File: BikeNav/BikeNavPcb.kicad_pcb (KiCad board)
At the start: 2 copper layers, 12 parts, among them J9 1.8 TFT SPi 128x160 pins, SW1 SW_DPST_x2, U1 TP4056, U2 ESP32-C3_SUPERMINI_TH

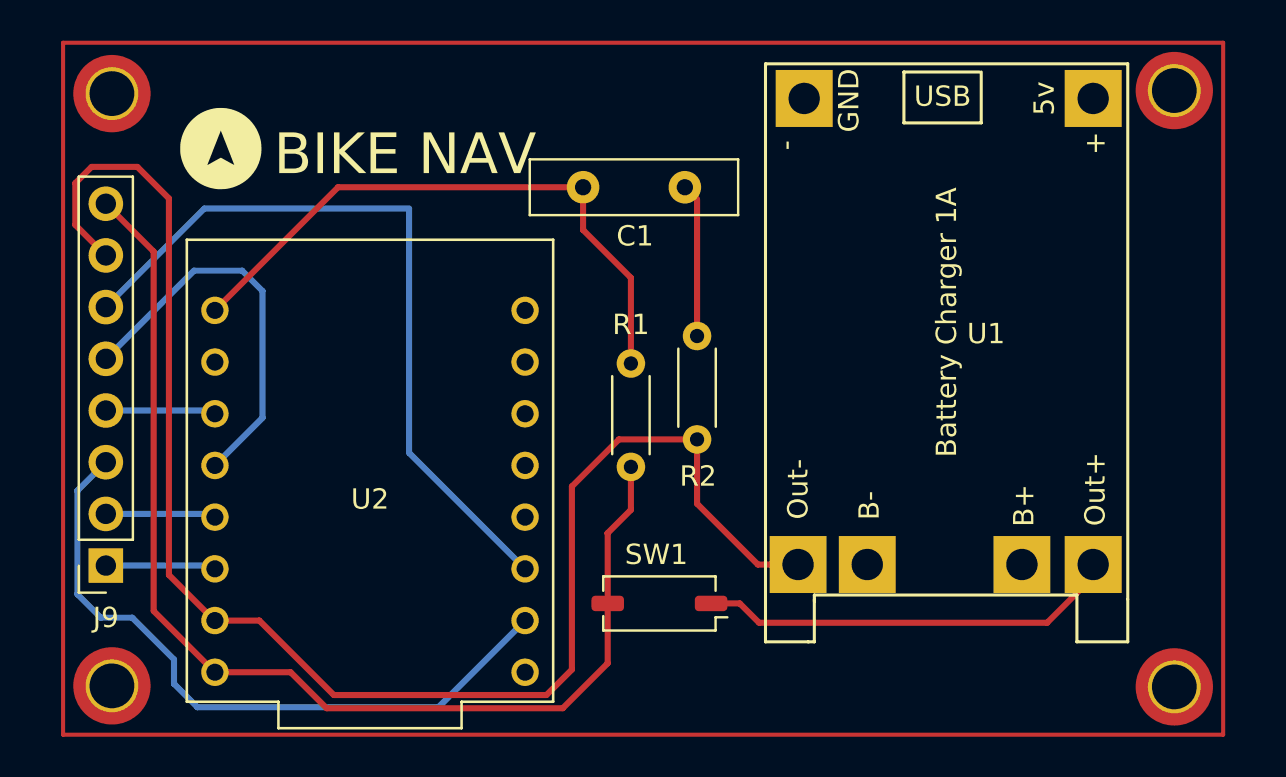
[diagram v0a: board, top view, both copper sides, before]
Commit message: Added Accurate dimesnsions for TFT mounting Holes and general optimization for Route Tracks.
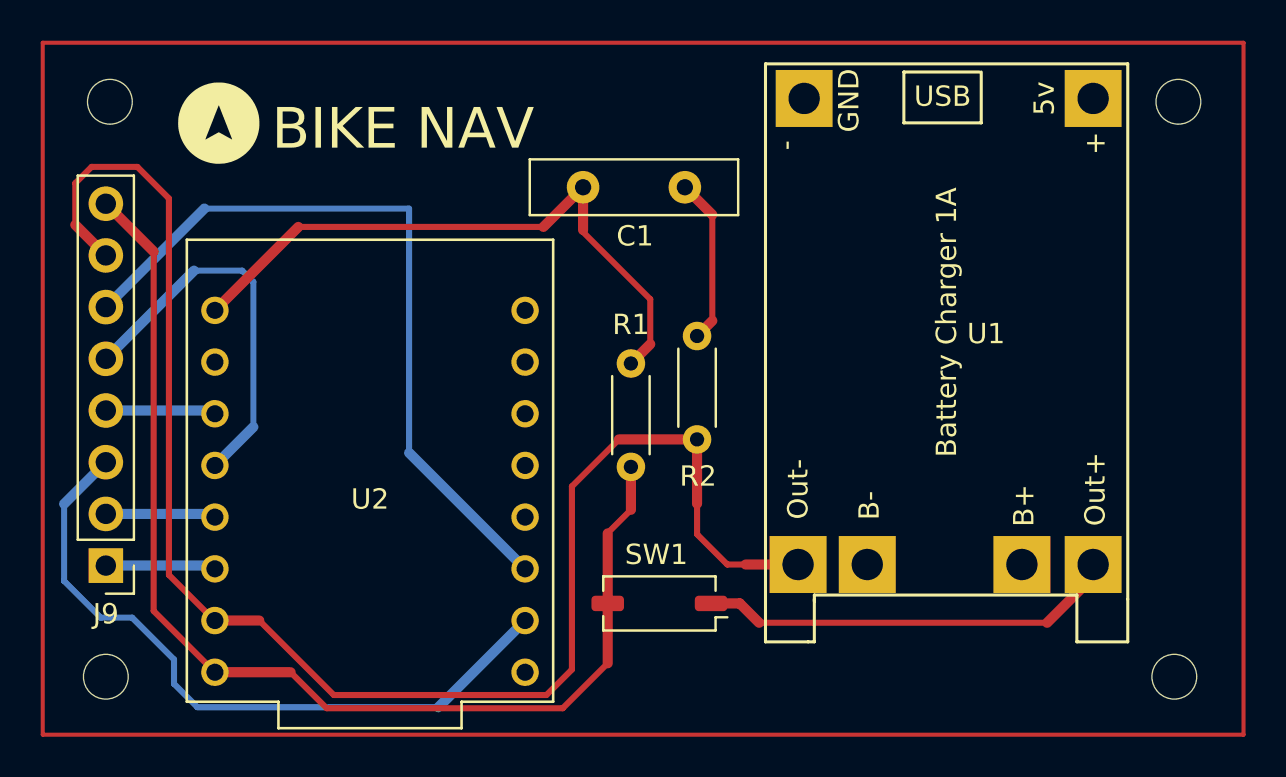
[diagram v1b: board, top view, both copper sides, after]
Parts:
- removed the REF** at (120.4, 113.6)
- removed the REF** at (172.6, 113.7)
- removed the REF** at (120.4, 84.5)
- removed the REF** at (172.6, 84.3)
- added REF**: MountingHole_2.2mm_M2, MountingHole:MountingHole_2.2mm_M2, F.Cu at (120.3, 84.9)
- added REF**: MountingHole_2.2mm_M2, MountingHole:MountingHole_2.2mm_M2, F.Cu at (172.6, 113.2)
- added REF**: MountingHole_2.2mm_M2, MountingHole:MountingHole_2.2mm_M2, F.Cu at (120.1, 113.2)
- added REF**: MountingHole_2.2mm_M2, MountingHole:MountingHole_2.2mm_M2, F.Cu at (172.8, 84.9)
- J9: footprint Connector_PinSocket_2.54mm:PinSocket_1x08_P2.54mm_Vertical -> Connector_PinHeader_2.54mm:PinHeader_1x08_P2.54mm_Vertical
- moved G*** 1.25 mm to (125.7, 86.0)
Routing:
- net Net-(C1-Pad2): track 7.56 -> 9.03 mm
- net /OUT-: track 76.5 -> 77.4 mm
- net /BATT EST: track 30.2 -> 31.0 mm
- net /SDA: track 33.8 -> 34.4 mm

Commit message: Added Accurate Dimension for TFT Display Mounting Holes and Step File for it.
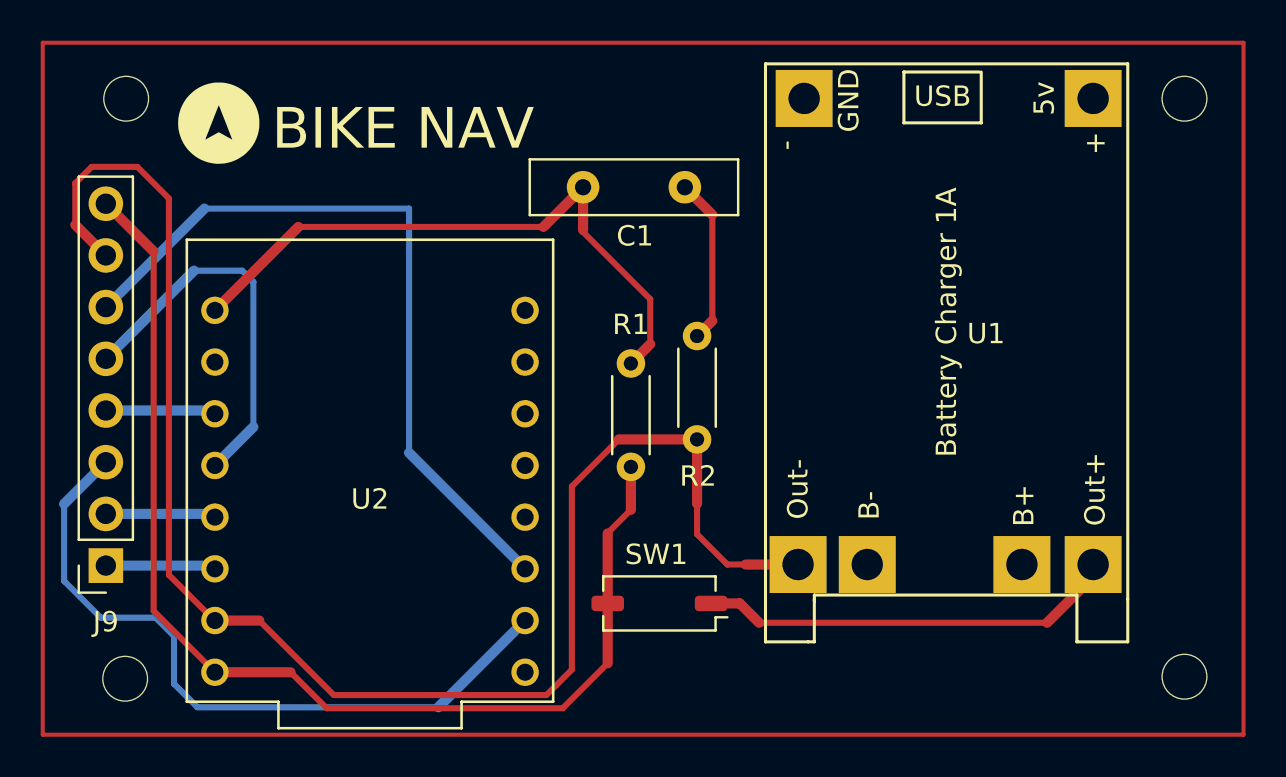
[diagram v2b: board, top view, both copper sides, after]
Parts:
- J9: footprint Connector_PinHeader_2.54mm:PinHeader_1x08_P2.54mm_Vertical -> Connector_PinSocket_2.54mm:PinSocket_1x08_P2.54mm_Vertical
- moved REF** 0.96 mm to (121.0, 113.2)
- moved REF** 0.81 mm to (121.1, 84.8)
- moved REF** 0.50 mm to (173.1, 113.2)
- moved REF** 0.34 mm to (173.1, 84.8)
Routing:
- net /SDA: track 34.4 -> 35.0 mm
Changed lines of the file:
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@@
 	(footprint "MountingHole:MountingHole_2.2mm_M2"
 		(layer "F.Cu")
-		(at 120.3 84.9)
+		(at 121.1 84.75)
 		(descr "Mounting Hole 2.2mm, M2, no annular, generated by kicad-footprint-generator mountinghole.py")
 		(tags "mountinghole M2")
@@
 		(embedded_fonts no)
 	)
-	(footprint "Connector_PinHeader_2.54mm:PinHeader_1x08_P2.54mm_Vertical"
+	(footprint "Connector_PinSocket_2.54mm:PinSocket_1x08_P2.54mm_Vertical"
 		(layer "F.Cu")
 		(at 120.1 107.69 180)
-		(descr "Through hole straight pin header, 1x08, 2.54mm pitch, single row")
-		(tags "Through hole pin header THT 1x08 2.54mm single row")
+		(descr "Through hole straight socket strip, 1x08, 2.54mm pitch, single row (from Kicad 4.0.7), script generated")
+		(tags "Through hole socket strip THT 1x08 2.54mm single row")
 		(property "Reference" "J9"
-			(at 0 -2.38 180)
+			(at 0 -2.77 180)
 			(layer "F.SilkS")
 			(effects
@@
 		)
 		(property "Value" "1.8 TFT SPi 128x160 pins"
-			(at 0 20.16 180)
+			(at 0 20.55 180)
 			(layer "F.Fab")
 			(effects
@@
 		(duplicate_pad_numbers_are_jumpers no)
 		(fp_line
-			(start 1.38 1.27)
-			(end 1.38 19.16)
+			(start 1.33 1.27)
+			(end 1.33 19.11)
 			(stroke
 				(width 0.12)
@@
 		)
 		(fp_line
-			(start -1.38 19.16)
-			(end 1.38 19.16)
+			(start 1.33 -1.33)
+			(end 1.33 0)
 			(stroke
 				(width 0.12)
@@
 		)
 		(fp_line
-			(start -1.38 1.27)
-			(end 1.38 1.27)
+			(start 0 -1.33)
+			(end 1.33 -1.33)
 			(stroke
 				(width 0.12)
@@
 		)
 		(fp_line
-			(start -1.38 1.27)
-			(end -1.38 19.16)
+			(start -1.33 19.11)
+			(end 1.33 19.11)
 			(stroke
 				(width 0.12)
@@
 		)
 		(fp_line
-			(start -1.38 0)
-			(end -1.38 -1.38)
+			(start -1.33 1.27)
+			(end 1.33 1.27)
 			(stroke
 				(width 0.12)
@@
 		)
 		(fp_line
-			(start -1.38 -1.38)
-			(end 0 -1.38)
+			(start -1.33 1.27)
+			(end -1.33 19.11)
 			(stroke
 				(width 0.12)
@@
 			(layer "F.SilkS")
 		)
-		(fp_rect
+		(fp_line
+			(start 1.77 19.55)
+			(end -1.77 19.55)
+			(stroke
+				(width 0.05)
+				(type solid)
+			)
+			(layer "F.CrtYd")
+		)
+		(fp_line
+			(start 1.77 -1.77)
+			(end 1.77 19.55)
+			(stroke
+				(width 0.05)
+				(type solid)
+			)
+			(layer "F.CrtYd")
+		)
+		(fp_line
+			(start -1.77 19.55)
+			(end -1.77 -1.77)
+			(stroke
+				(width 0.05)
+				(type solid)
+			)
+			(layer "F.CrtYd")
+		)
+		(fp_line
 			(start -1.77 -1.77)
-			(end 1.77 19.55)
+			(end 1.77 -1.77)
 			(stroke
 				(width 0.05)
 				(type solid)
 			)
-			(fill no)
 			(layer "F.CrtYd")
 		)
@@
 		)
 		(fp_line
-			(start 1.27 -1.27)
+			(start 1.27 -0.635)
 			(end 1.27 19.05)
 			(stroke
@@
 		)
 		(fp_line
-			(start -0.635 -1.27)
-			(end 1.27 -1.27)
+			(start 0.635 -1.27)
+			(end 1.27 -0.635)
 			(stroke
 				(width 0.1)
@@
 		(fp_line
 			(start -1.27 19.05)
-			(end -1.27 -0.635)
+			(end -1.27 -1.27)
 			(stroke
 				(width 0.1)
@@
 		)
 		(fp_line
-			(start -1.27 -0.635)
-			(end -0.635 -1.27)
+			(start -1.27 -1.27)
+			(end 0.635 -1.27)
 			(stroke
 				(width 0.1)
@@
 		)
 		(embedded_fonts no)
-		(model "${KICAD10_3DMODEL_DIR}/Connector_PinHeader_2.54mm.3dshapes/PinHeader_1x08_P2.54mm_Vertical.step"
+		(model "${KICAD10_3DMODEL_DIR}/Connector_PinSocket_2.54mm.3dshapes/PinSocket_1x08_P2.54mm_Vertical.step"
 			(offset
 				(xyz 0 0 0)
@@
 			)
 			(rotate
-				(xyz 0 0 0)
-			)
-		)
-		(model "${KICAD10_3DMODEL_DIR}/LCD_TFT_1.8_SPI_ST7735/LCD_TFT_1.8_SPI_ST7735.step"
-			(hide yes)
+				(xyz -0 -0 -0)
+			)
+		)
+		(model "${KICAD10_3DMODEL_DIR}/LCD_TFT_1.8_SPI_ST7735/TFT LCD 1.8 inch ST7735.step"
 			(offset
-				(xyz -27 -8 6)
+				(xyz 2 8.5 11)
 			)
 			(scale
@@
 			)
 			(rotate
-				(xyz -90 -0 -0)
+				(xyz 180 180 -0)
 			)
 		)
@@
 	(footprint "MountingHole:MountingHole_2.2mm_M2"
 		(layer "F.Cu")
-		(at 172.6 113.15)
+		(at 173.1 113.15)
 		(descr "Mounting Hole 2.2mm, M2, no annular, generated by kicad-footprint-generator mountinghole.py")
 		(tags "mountinghole M2")
@@
 	(footprint "MountingHole:MountingHole_2.2mm_M2"
 		(layer "F.Cu")
-		(at 120.1 113.15)
+		(at 121.05 113.25)
 		(descr "Mounting Hole 2.2mm, M2, no annular, generated by kicad-footprint-generator mountinghole.py")
 		(tags "mountinghole M2")
@@
 	(footprint "MountingHole:MountingHole_2.2mm_M2"
 		(layer "F.Cu")
-		(at 172.8 84.9)
+		(at 173.1 84.75)
 		(descr "Mounting Hole 2.2mm, M2, no annular, generated by kicad-footprint-generator mountinghole.py")
 		(tags "mountinghole M2")
@@
 	)
 	(segment
+		(start 119.85 110.25)
+		(end 122.55 110.25)
+		(width 0.3)
+		(layer "B.Cu")
+		(net "/SDA")
+	)
+	(segment
+		(start 123.45 111.15)
+		(end 123.45 113.5)
+		(width 0.3)
+		(layer "B.Cu")
+		(net "/SDA")
+	)
+	(segment
+		(start 136.44 114.65)
+		(end 140.7 110.39)
+		(width 0.5)
+		(layer "B.Cu")
+		(net "/SDA")
+	)
+	(segment
 		(start 118.05 108.45)
 		(end 119.85 110.25)
@@
 	)
 	(segment
-		(start 123.45 112.3)
-		(end 123.45 113.5)
+		(start 124.6 114.65)
+		(end 136.44 114.65)
+		(width 0.3)
+		(layer "B.Cu")
+		(net "/SDA")
+	)
+	(segment
+		(start 118.05 104.66)
+		(end 118.05 108.45)
 		(width 0.3)
 		(layer "B.Cu")
@@
 	)
 	(segment
-		(start 136.44 114.65)
-		(end 140.7 110.39)
-		(width 0.5)
-		(layer "B.Cu")
-		(net "/SDA")
-	)
-	(segment
-		(start 118.05 104.66)
-		(end 118.05 108.45)
+		(start 122.55 110.25)
+		(end 123.45 111.15)
 		(width 0.3)
 		(layer "B.Cu")
-		(net "/SDA")
-	)
-	(segment
-		(start 119.85 110.25)
-		(end 121.4 110.25)
-		(width 0.3)
-		(layer "B.Cu")
-		(net "/SDA")
-	)
-	(segment
-		(start 121.4 110.25)
-		(end 123.45 112.3)
-		(width 0.3)
-		(layer "B.Cu")
-		(net "/SDA")
-	)
-	(segment
-		(start 124.6 114.65)
-		(end 136.44 114.65)
-		(width 0.3)
-		(layer "B.Cu")

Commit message: Revised Silkscreen for Logo.
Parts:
- moved G*** 0.16 mm to (125.7, 86.1)

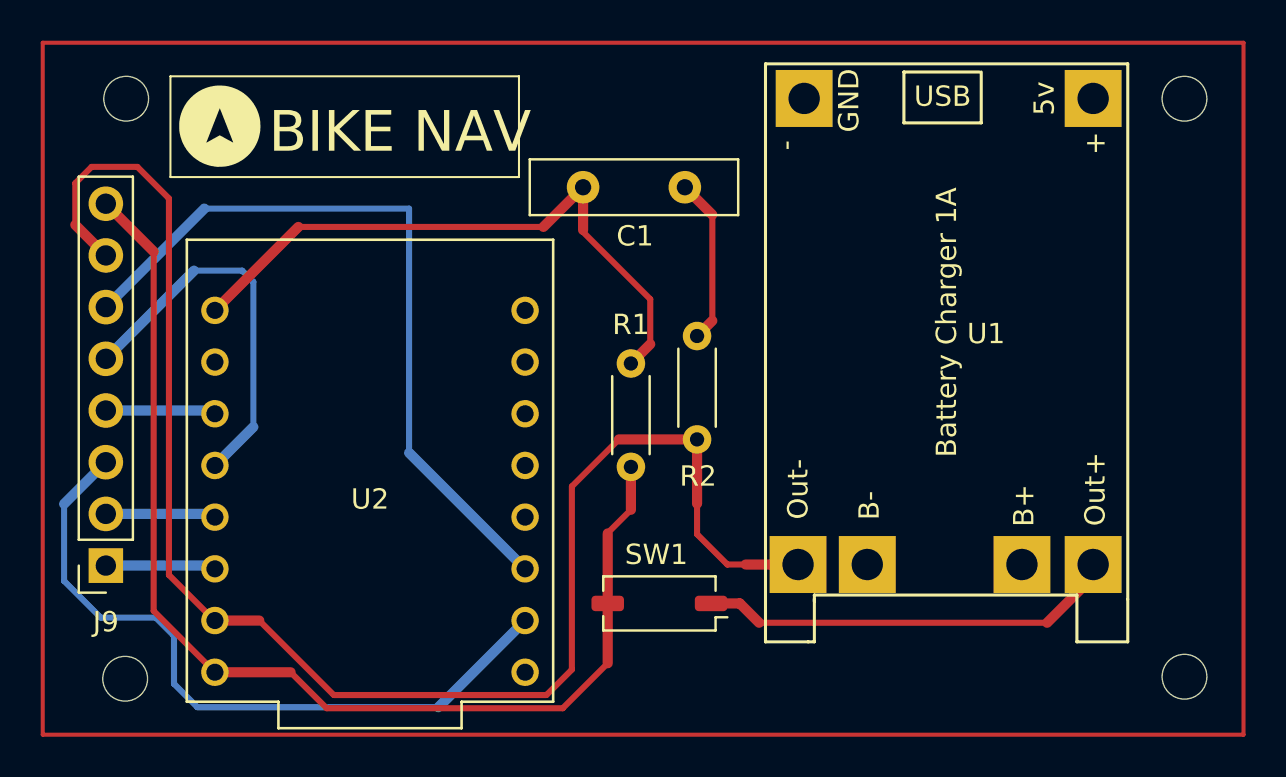
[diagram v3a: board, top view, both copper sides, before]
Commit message: Added New Compact Footprint for THT Capacitor and 3d Model.
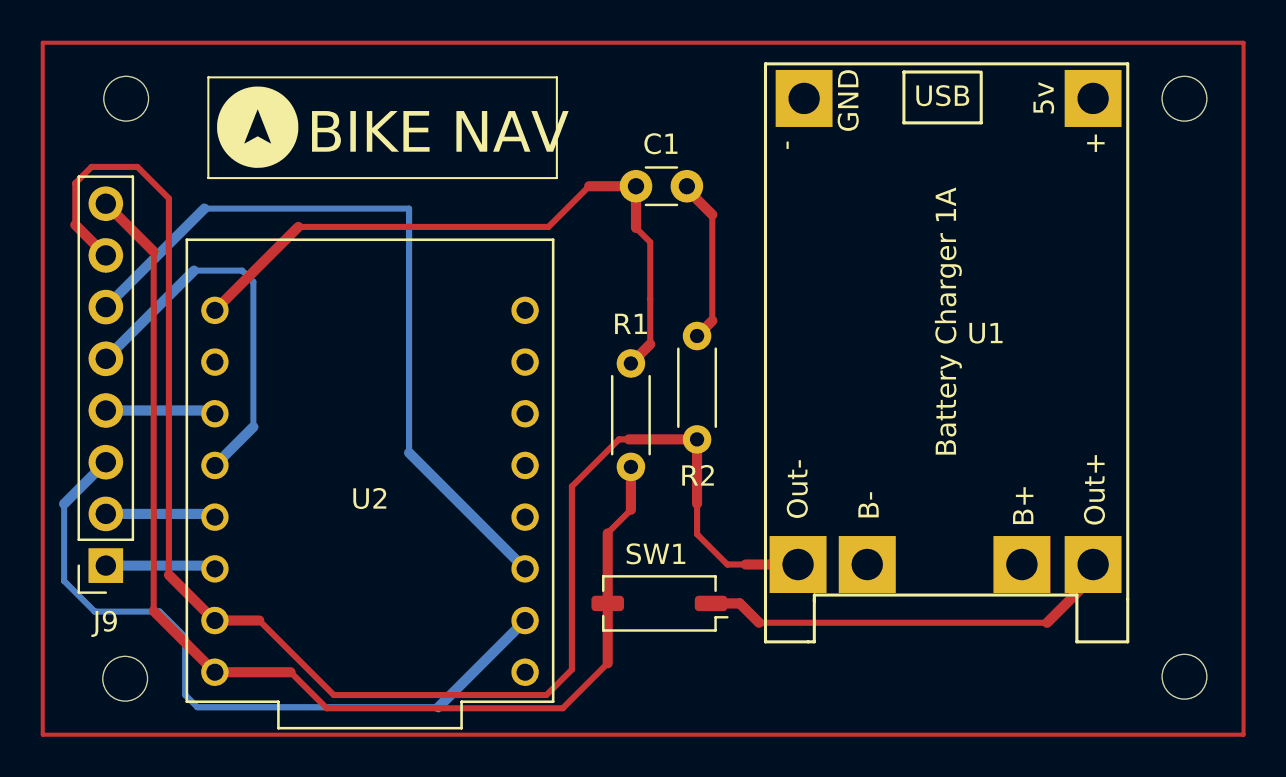
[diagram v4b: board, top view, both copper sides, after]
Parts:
- C1: footprint Capacitor_THT:C_Disc_D10.0mm_W2.5mm_P5.00mm -> Capacitor_THT:C_Disc_D3.0mm_W1.6mm_P2.50mm
- moved C1 2.60 mm to (146.2, 89.0)
- moved G*** 1.86 mm to (127.6, 86.2)
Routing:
- net /BATT EST: track 31.0 -> 32.6 mm
- net Net-(C1-Pad2): track 9.03 -> 8.18 mm
